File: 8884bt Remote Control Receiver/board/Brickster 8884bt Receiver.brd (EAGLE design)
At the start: 28.8 x 28.8 mm, 22 parts, among them J1 AVR_SPI_PRG_6NS, J2 CON_PF, J3 CON_PF, J4 CON_PF, U1 IC_ATTINY_X4A, U2 IC_TB6612FNG, U3 IC_RT9164A, U4 BLUETOOTH-RN41"

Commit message: Update receiver to revision 1a
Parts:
- removed B1, B2: B_CDBHM240L-HF, brickster:MBS-2
- removed C4: 0.1uF, brickster:0402
- removed D2: D, brickster:SOD80
- added Q1, Q2: IC_FET_BRIDGESO8, brickster:SO8
- B3, B4: value B_MDB8S -> B_CDBHM240L-HF; device brickster:MICRO-DIP -> brickster:MBS-2
- C1, C3, R1: device brickster:0402 -> brickster:0805
- R2: value 1k -> 3.3k; device brickster:0402 -> brickster:0805
- moved C2 20.7 mm to (14.4, 24.6), turned to 270 degrees
- moved U3 20.3 mm to (14.4, 24.3), turned to 0 degrees
- moved D1 17.5 mm to (1.35, 4.14)
- moved R2 13.3 mm to (5.93, 4.86), flipped to the bottom
- moved C1 11.9 mm to (16.7, 24.6), flipped to the bottom, turned to 270 degrees
- moved C3 8.09 mm to (26.7, 3.05), turned to 270 degrees
- moved R1 3.26 mm to (11.6, 22.2), flipped to the bottom, turned to 270 degrees
- moved B4 2.84 mm to (22.4, 5.94), turned to 0 degrees
- moved C5 2.16 mm to (26.5, 7.85), turned to 270 degrees
- moved B3 1.50 mm to (5.49, 6.05), turned to 0 degrees
- moved U1 0.96 mm to (14.2, 15.7), turned to 90 degrees
- moved J2 0.46 mm to (14.8, 1.02)
- moved J3 0.46 mm to (5.49, 1.02)
- moved J4 0.08 mm to (22.3, 1.02)
- turned U2 to 0 degrees
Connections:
- removed net N$1: D2.1, J1.2
- new net PF_GND: J2.GND, Q1.P$2, Q1.P$4, Q1.P$5
- net 3.3V: now also J1.2, R1.P$2, U3.4; no longer C4.1, R1.2
- net A01: now also B3.AC2; no longer B3.AC1
- net A02: now also B3.AC1; no longer B3.AC2
- net AIN1: now also U1.12; no longer U1.5
- net AIN2: now also U1.11; no longer U1.3
- net ATRX/BTTX: now also U1.2; no longer U1.11
- net ATTX/BTRX: now also U1.3; no longer U1.6
- net B01: now also B4.AC2; no longer B4.AC1
- net B02: now also B4.AC1; no longer B4.AC2
- net BIN1: now also U1.13; no longer U1.10
- net BIN2: now also U1.5; no longer U1.12
- net BLUE: now also D1.2, D1.3; no longer D1.1, D1.4
- net GND: now also C1.P$2, C3.P$2, Q1.P$3, Q2.P$3; no longer B1.-, B1.AC2, B2.-, C1.2, C3.2, C4.2, J2.GND
- net N$15: now also R1.P$1; no longer R1.1
- net N$16: now also D1.1, D1.4, R2.P$1; no longer D1.2, D1.3, R2.1
- net ORANGE: now also R2.P$2; no longer R2.2
- net PF_9V: now also Q1.P$1, Q1.P$6, Q1.P$8; no longer B1.AC1
- net PF_C1: now also Q2.P$1, Q2.P$6, Q2.P$8; no longer B2.AC2
- net PF_C2: now also Q2.P$2, Q2.P$4, Q2.P$5; no longer B2.AC1
- net PWMA: now also U1.10; no longer U1.2
- net PWMB: now also U1.6; no longer U1.13
- net VIN: now also C1.P$1, C3.P$1, Q1.P$7, Q2.P$7; no longer B1.+, B2.+, C1.1, C3.1, D2.2
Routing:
- net N$1: track 16.5 -> 0.00 mm
- net VIN: track 63.2 -> 79.3 mm, vias 3 -> 7
- net PF_GND: track 0.00 -> 15.8 mm, vias 0 -> 1
- net A01: track 42.8 -> 28.7 mm
- net GND: track 9.02 -> 22.4 mm, vias 17 -> 10
- net MOSI: track 8.83 -> 21.8 mm
- net A02: track 47.8 -> 36.1 mm
- net PF_9V: track 8.05 -> 17.5 mm
- net ATTX/BTRX: track 27.9 -> 18.7 mm, vias 1 -> 2
- net B02: track 23.6 -> 14.9 mm, vias 4 -> 0
- net PWMB: track 8.04 -> 16.3 mm
- net 3.3V: track 54.9 -> 62.9 mm, vias 3 -> 2
- net MISO: track 11.2 -> 19.0 mm, vias 1 -> 2
- net BIN1: track 14.4 -> 21.1 mm
- net BIN2: track 10.6 -> 16.9 mm
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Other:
- outline, holes or cut-outs redrawn
- board text added: "rev. 1a"
- board text removed: "rev. 1"

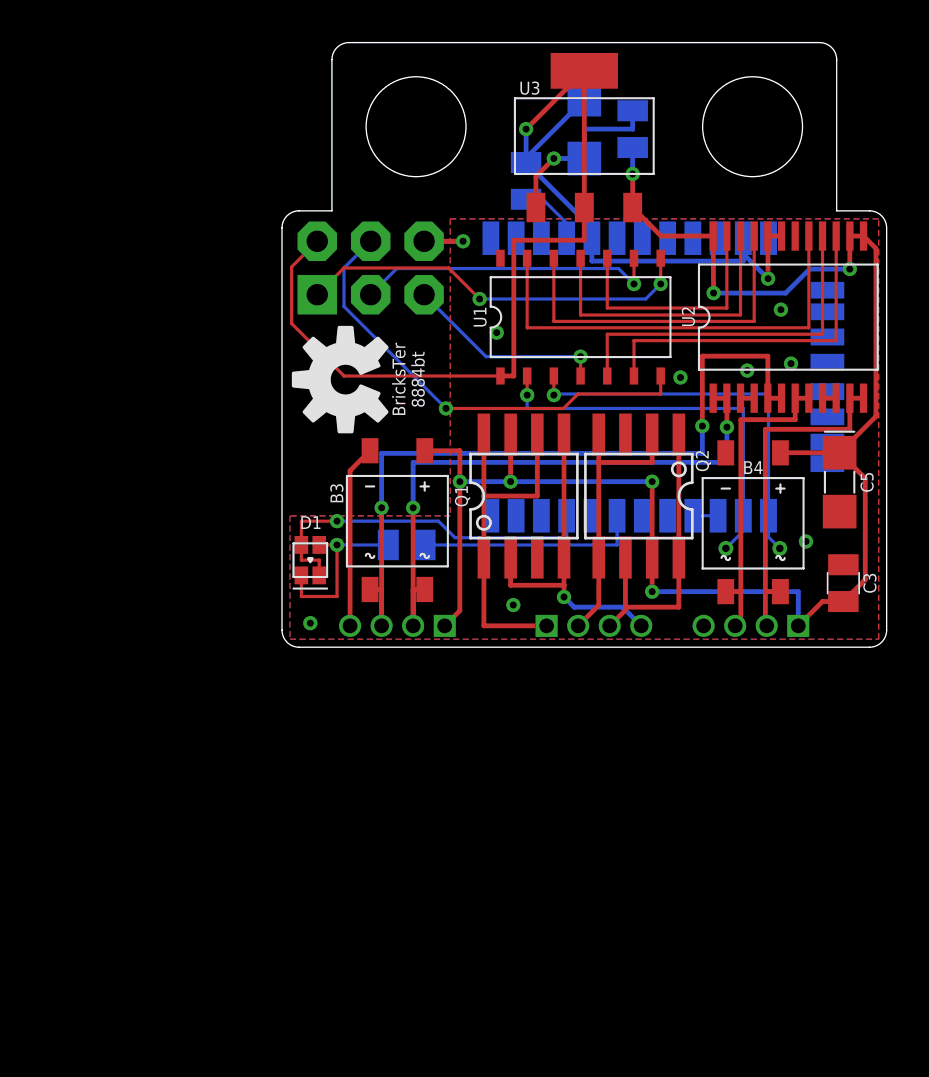
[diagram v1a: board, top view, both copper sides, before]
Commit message: Add drv8833 to library and schematic
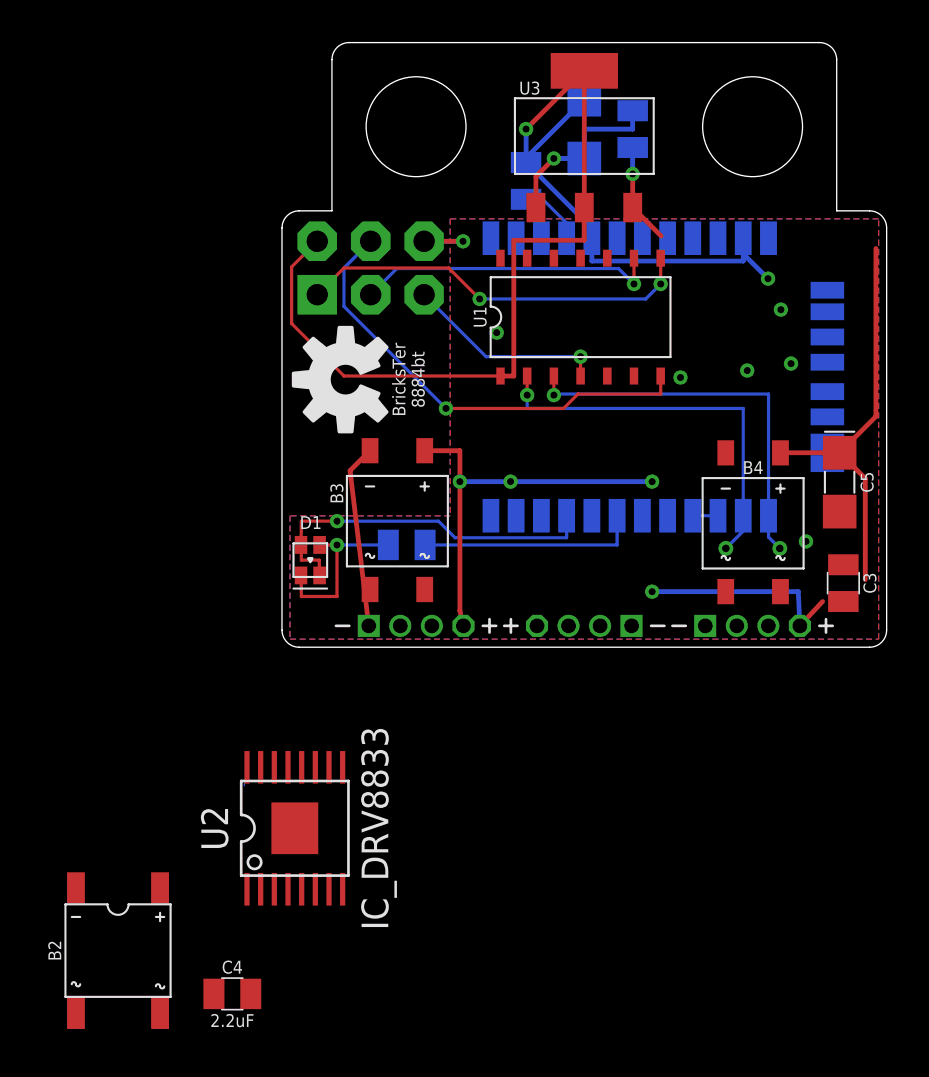
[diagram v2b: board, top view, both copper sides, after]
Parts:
- removed Q1, Q2: IC_FET_BRIDGESO8, brickster:SO8
- added B2: B_MDB8S, brickster:MICRO-DIP
- added C4: 2.2uF, brickster:0805
- C3: value 0.1uF -> 0.01uF
- U2: value IC_TB6612FNG -> IC_DRV8833; device brickster:SSOP24 -> brickster:PWP_R-PDSO-G16
- moved U2 33.8 mm to (0.61, -8.61)
- moved J3 0.89 mm to (6.38, 1.02)
- moved J2 0.46 mm to (14.4, 1.02)
- moved J4 0.08 mm to (22.4, 1.02)
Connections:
- removed net PF_9V: J2.9V, Q1.P$1, Q1.P$6, Q1.P$8
- removed net PF_GND: J2.GND, Q1.P$2, Q1.P$4, Q1.P$5
- removed net PWMA: U1.10, U2.23
- removed net PWMB: U1.6, U2.15
- new net N$1: C3.P$2, U2.11
- new net N$2: C4.P$2, U2.14
- net 3.3V: now also U2.1; no longer U2.19, U2.20
- net A01: no longer U2.1
- net A02: now also U2.4; no longer U2.5, U2.6
- net AIN1: now also U2.16; no longer U2.21
- net AIN2: now also U2.15; no longer U2.22
- net B01: now also U2.7; no longer U2.11, U2.12
- net B02: now also U2.5; no longer U2.7, U2.8
- net BIN1: now also U2.9; no longer U2.17
- net BIN2: now also U2.10; no longer U2.16
- net GND: now also B2.-, C4.P$1, J2.GND, U2.13, U2.17, U2.6; no longer C3.P$2, Q1.P$3, Q2.P$3, U2.10, U2.18, U2.4, U2.9
- net PF_C1: now also B2.AC1; no longer Q2.P$1, Q2.P$6, Q2.P$8
- net PF_C2: now also B2.AC2; no longer Q2.P$2, Q2.P$4, Q2.P$5
- net VIN: now also B2.+, J2.9V, U2.12; no longer Q1.P$7, Q2.P$7, U2.13, U2.14, U2.24
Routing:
- net A02: track 36.1 -> 0.00 mm, vias 2 -> 0
- net A01: track 28.7 -> 0.00 mm, vias 2 -> 0
- net VIN: track 79.3 -> 53.9 mm, vias 7 -> 5
- net BIN1: track 21.1 -> 0.00 mm
- net PF_9V: track 17.5 -> 0.00 mm
- net BIN2: track 16.9 -> 0.00 mm
- net AIN1: track 16.6 -> 0.00 mm
- net PWMB: track 16.3 -> 0.00 mm
- net B01: track 16.2 -> 0.00 mm
- net PF_GND: track 15.8 -> 0.00 mm, vias 1 -> 0
- net B02: track 14.9 -> 0.00 mm
- net PF_C1: track 14.3 -> 0.00 mm
- net AIN2: track 14.1 -> 0.00 mm
- net PF_C2: track 13.4 -> 0.00 mm
- net PWMA: track 11.5 -> 0.00 mm
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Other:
- board text added: "rev. 2"
- board text removed: "rev. 1a"

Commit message: Route rev. 2 board
Need to change OSH logo to t/b-stop
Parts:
- removed R1: 10K, brickster:0805
- added LOGO2: OSHW-LOGOM, SparkFun-Aesthetics:OSHW-LOGO-M
- B2: value B_MDB8S -> B_CDBHM240L-HF; device brickster:MICRO-DIP -> brickster:MBS-2
- D1: value Blue/Orange -> LED0805; device brickster:CHIP-LTST -> brickster:0805_POL
- U4: value BLUETOOTH-RN41" -> HC-06; device SparkFun-RF:RN41 -> brickster:BLUETOOTH_SMD
- moved C4 43.3 mm to (22.4, 19.1)
- moved U2 32.5 mm to (23.6, 14.3)
- moved B2 31.9 mm to (16.7, 5.94), turned to 180 degrees
- moved U3 17.7 mm to (10.6, 6.99), turned to 180 degrees
- moved LOGO1 17.0 mm to (14.4, 25.4), turned to 0 degrees
- moved C1 16.7 mm to (6.92, 11.0), flipped to the top
- moved C3 15.3 mm to (27.2, 18.4), turned to 90 degrees
- moved C2 13.5 mm to (19.4, 12.1), flipped to the top, turned to 90 degrees
- moved C5 12.3 mm to (19.6, 18.0)
- moved D1 5.51 mm to (6.86, 4.11)
- moved U4 3.84 mm to (12.7, 12.9), turned to 270 degrees
- moved B3 2.64 mm to (2.84, 5.94)
- moved U1 2.27 mm to (12.0, 16.1)
- moved J1 1.97 mm to (2.69, 16.8), turned to 90 degrees
- moved R2 1.19 mm to (6.86, 4.11), turned to 180 degrees
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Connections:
- removed net BLUE: D1.2, D1.3, U4.21
- removed net N$15: R1.P$1, U4.4
- removed net N$16: D1.1, D1.4, R2.P$1
- removed net N$7: U4.15, U4.16
- removed net ORANGE: R2.P$2, U4.19
- new net BTRST: U1.10, U4.11
- new net KEY: U1.11, U4.26
- new net LED: R2.P$1, U4.24
- new net N$3: U4.3, U4.4
- new net N$4: D1.P$2, R2.P$2
- net 3.3V: now also U4.12; no longer R1.P$2, U4.11, U4.5
- net A01: now also B3.AC1; no longer B3.AC2
- net A02: now also B3.AC2; no longer B3.AC1
- net AIN1: now also U1.2; no longer U1.12
- net AIN2: now also U1.3; no longer U1.11
- net ATRX/BTTX: now also U1.13, U4.1; no longer U1.2, U4.14
- net ATTX/BTRX: now also U1.12, U4.2; no longer U1.3, U4.13
- net BIN1: now also U1.6; no longer U1.13
- net GND: now also D1.P$1, U4.13, U4.21, U4.22; no longer U4.1, U4.12, U4.28, U4.29
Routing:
- net A01: track 0.00 -> 31.8 mm, vias 0 -> 2
- net A02: track 0.00 -> 30.9 mm, vias 0 -> 2
- net KEY: track 0.00 -> 20.9 mm, vias 0 -> 1
- net 3.3V: track 60.2 -> 41.6 mm, vias 2 -> 1
- net BLUE: track 17.4 -> 0.00 mm, vias 1 -> 0
- net LED: track 0.00 -> 16.9 mm
- net AIN1: track 0.00 -> 16.8 mm
- net BIN2: track 0.00 -> 15.1 mm
- net ATRX/BTTX: track 18.8 -> 3.97 mm, vias 2 -> 1
- net ATTX/BTRX: track 18.7 -> 3.89 mm, vias 2 -> 1
- net BIN1: track 0.00 -> 14.8 mm, vias 0 -> 2
- net AIN2: track 0.00 -> 14.6 mm
- net B02: track 0.00 -> 14.6 mm, vias 0 -> 2
- net BTRST: track 0.00 -> 13.3 mm, vias 0 -> 1
- net VIN: track 53.9 -> 67.1 mm, vias 5 -> 3
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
